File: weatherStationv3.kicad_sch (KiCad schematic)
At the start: 52 parts, among them J1 5-16V, J10 ANTENNA, J11 RS485_TERM, J2 USB_PWR_IN, J3 PORT1, J4 PORT2, J5 PORT3, J6 PORT4, J7 3.3-5V, J8 I2C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

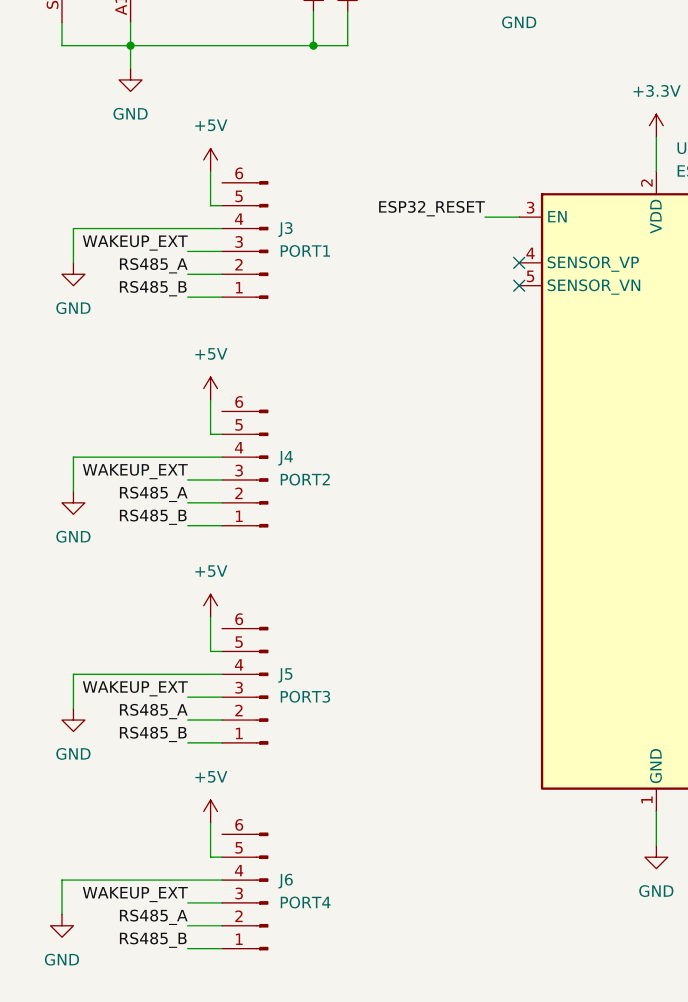
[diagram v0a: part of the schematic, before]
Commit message: changeport connectors, move lora module, and impedance-match antenna
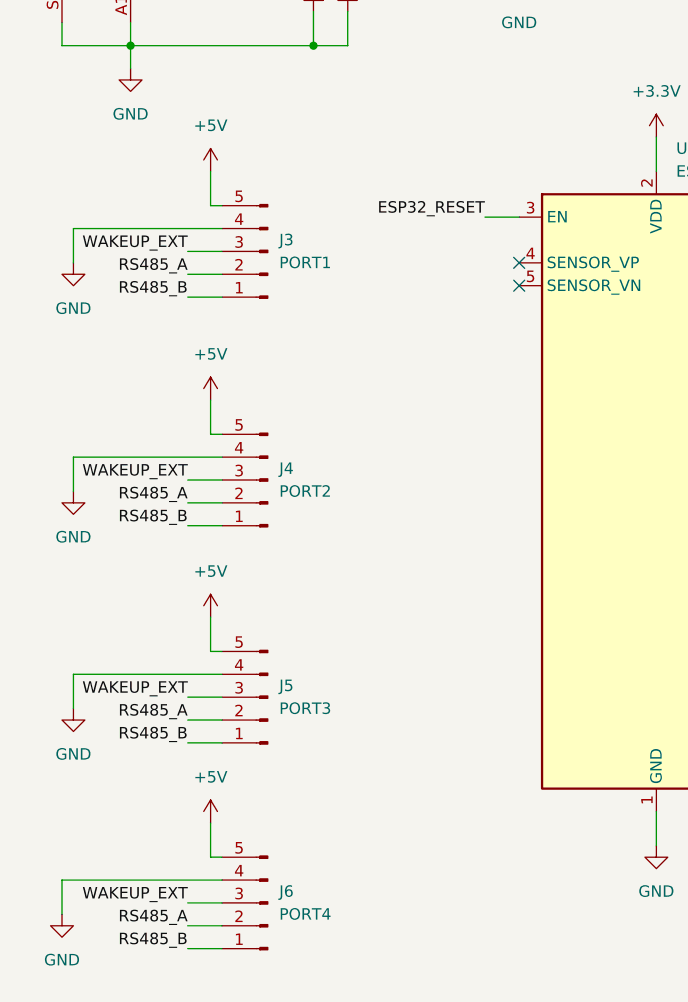
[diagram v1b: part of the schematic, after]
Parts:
- J3, J4, J5, J6: footprint Connector_Molex:Molex_KK-254_AE-6410-06A_1x06_P2.54mm_Vertical -> Connector_JST:JST_XH_B5B-XH-A_1x05_P2.50mm_Vertical; symbol Connector:Conn_01x06_Pin -> Connector:Conn_01x05_Pin
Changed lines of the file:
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@@
 	)
 	(symbol
-		(lib_id "Connector:Conn_01x06_Pin")
+		(lib_id "Connector:Conn_01x05_Pin")
 		(at 44.45 163.83 180)
 		(unit 1)
@@
 		(fields_autoplaced yes)
 		(property "Reference" "J5"
-			(at 45.72 161.2899 0)
+			(at 45.72 162.5599 0)
 			(effects
 				(font
@@
 		)
 		(property "Value" "PORT3"
-			(at 45.72 163.8299 0)
+			(at 45.72 165.0999 0)
 			(effects
 				(font
@@
 			)
 		)
-		(property "Footprint" "Connector_Molex:Molex_KK-254_AE-6410-06A_1x06_P2.54mm_Vertical"
+		(property "Footprint" "Connector_JST:JST_XH_B5B-XH-A_1x05_P2.50mm_Vertical"
 			(at 44.45 163.83 0)
 			(effects
@@
 			)
 		)
-		(property "Description" "Generic connector, single row, 01x06, script generated"
+		(property "Description" "Generic connector, single row, 01x05, script generated"
 			(at 44.45 163.83 0)
 			(effects
@@
 		(pin "4"
 		)
-		(pin "6"
-		)
 		(pin "3"
 		)
@@
 	)
 	(symbol
-		(lib_id "Connector:Conn_01x06_Pin")
+		(lib_id "Connector:Conn_01x05_Pin")
 		(at 44.45 114.3 180)
 		(unit 1)
@@
 		(fields_autoplaced yes)
 		(property "Reference" "J3"
-			(at 45.72 111.7599 0)
+			(at 45.72 113.0299 0)
 			(effects
 				(font
@@
 		)
 		(property "Value" "PORT1"
-			(at 45.72 114.2999 0)
+			(at 45.72 115.5699 0)
 			(effects
 				(font
@@
 			)
 		)
-		(property "Footprint" "Connector_Molex:Molex_KK-254_AE-6410-06A_1x06_P2.54mm_Vertical"
+		(property "Footprint" "Connector_JST:JST_XH_B5B-XH-A_1x05_P2.50mm_Vertical"
 			(at 44.45 114.3 0)
 			(effects
@@
 			)
 		)
-		(property "Description" "Generic connector, single row, 01x06, script generated"
+		(property "Description" "Generic connector, single row, 01x05, script generated"
 			(at 44.45 114.3 0)
 			(effects
@@
 		(pin "4"
 		)
-		(pin "6"
-		)
 		(pin "3"
 		)
@@
 	)
 	(symbol
-		(lib_id "Connector:Conn_01x06_Pin")
+		(lib_id "Connector:Conn_01x05_Pin")
 		(at 44.45 139.7 180)
 		(unit 1)
@@
 		(fields_autoplaced yes)
 		(property "Reference" "J4"
-			(at 45.72 137.1599 0)
+			(at 45.72 138.4299 0)
 			(effects
 				(font
@@
 		)
 		(property "Value" "PORT2"
-			(at 45.72 139.6999 0)
+			(at 45.72 140.9699 0)
 			(effects
 				(font
@@
 			)
 		)
-		(property "Footprint" "Connector_Molex:Molex_KK-254_AE-6410-06A_1x06_P2.54mm_Vertical"
+		(property "Footprint" "Connector_JST:JST_XH_B5B-XH-A_1x05_P2.50mm_Vertical"
 			(at 44.45 139.7 0)
 			(effects
@@
 			)
 		)
-		(property "Description" "Generic connector, single row, 01x06, script generated"
+		(property "Description" "Generic connector, single row, 01x05, script generated"
 			(at 44.45 139.7 0)
 			(effects
@@
 		(pin "4"
 		)
-		(pin "6"
-		)
 		(pin "3"
 		)
@@
 	)
 	(symbol
-		(lib_id "Connector:Conn_01x06_Pin")
+		(lib_id "Connector:Conn_01x05_Pin")
 		(at 44.45 186.69 180)
 		(unit 1)
@@
 		(fields_autoplaced yes)
 		(property "Reference" "J6"
-			(at 45.72 184.1499 0)
+			(at 45.72 185.4199 0)
 			(effects
 				(font
@@
 		)
 		(property "Value" "PORT4"
-			(at 45.72 186.6899 0)
+			(at 45.72 187.9599 0)
 			(effects
 				(font
@@
 			)
 		)
-		(property "Footprint" "Connector_Molex:Molex_KK-254_AE-6410-06A_1x06_P2.54mm_Vertical"
+		(property "Footprint" "Connector_JST:JST_XH_B5B-XH-A_1x05_P2.50mm_Vertical"
 			(at 44.45 186.69 0)
 			(effects
@@
 			)
 		)
-		(property "Description" "Generic connector, single row, 01x06, script generated"
+		(property "Description" "Generic connector, single row, 01x05, script generated"
 			(at 44.45 186.69 0)
 			(effects
@@
 		(pin "4"
 		)
-		(pin "6"
-		)
 		(pin "3"
